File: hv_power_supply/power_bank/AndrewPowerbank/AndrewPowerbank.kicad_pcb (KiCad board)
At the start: 2 copper layers, 48.3 x 30.5 mm, 51 parts, among them J1 NanoFit_RA_TH_02, J2 NanoFit_RA_TH_02, J3 USB-A-S-X-X-SM2, J4 USB-Micro-1981568-1, J5 NanoFit_RA_TH_02, Q1 SSM3K333R, U1 MCP73871T-2CCI_ML, U2 TPS61090RSAR

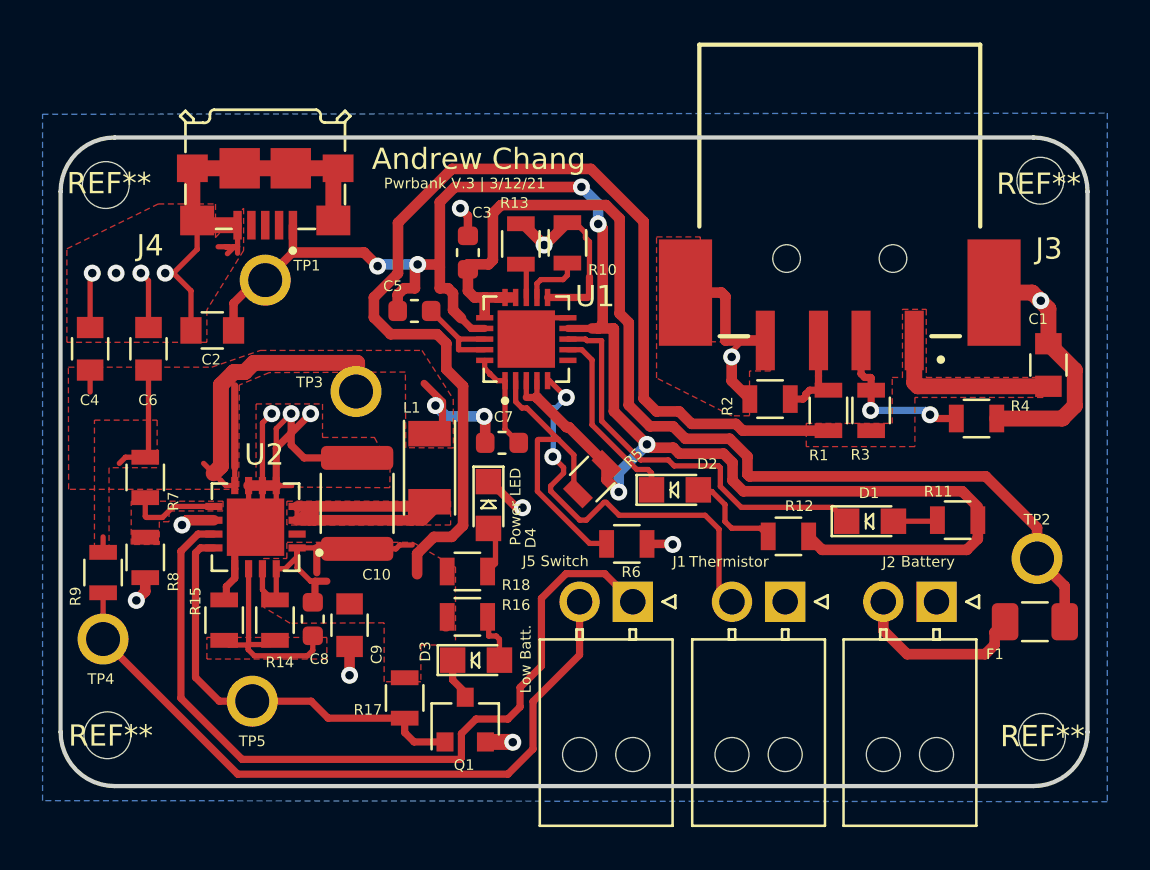
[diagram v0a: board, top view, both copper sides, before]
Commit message: Fix GND connection @ U2 Boost pin 13, 17
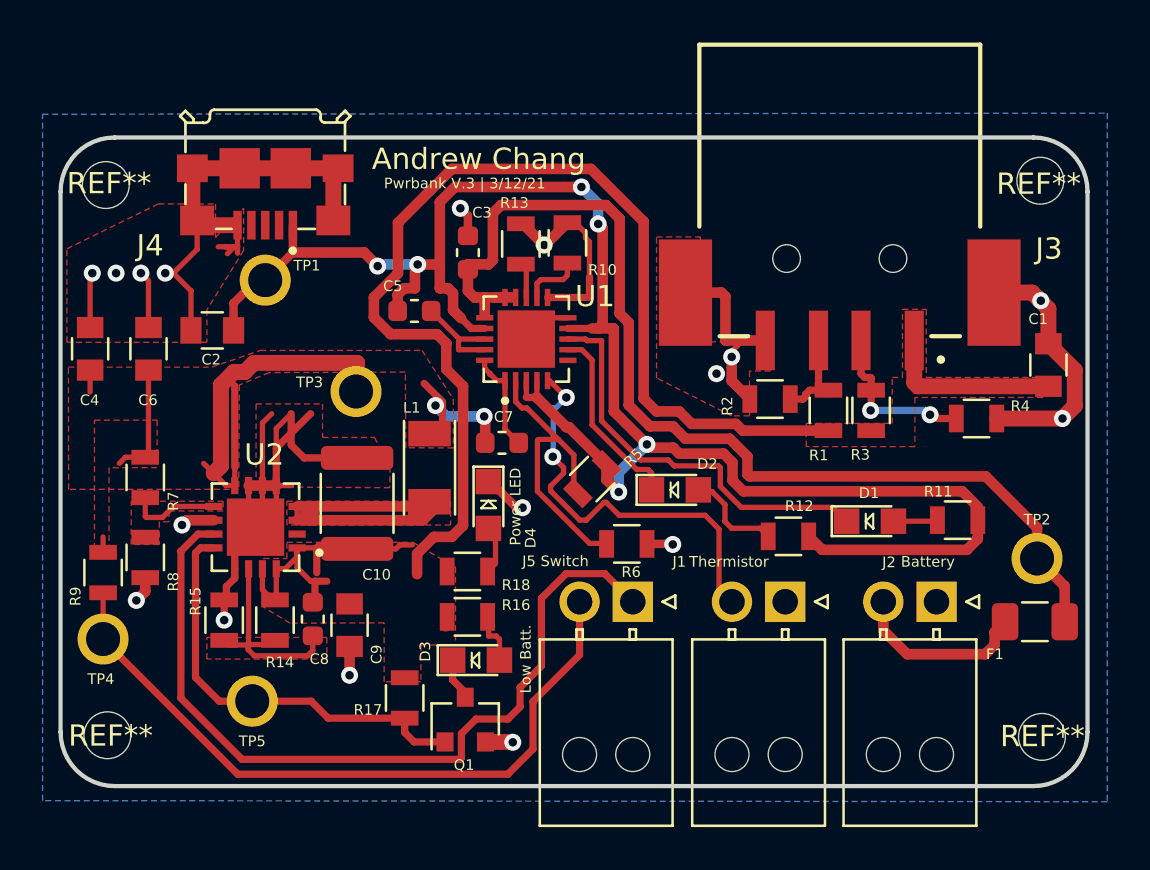
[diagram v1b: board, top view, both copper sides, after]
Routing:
- net GND: track 101.6 -> 102.6 mm

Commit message: Fix issues with board after feedback from Corey.
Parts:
- moved C1 3.60 mm to (74.5, 84.1), turned to 0 degrees
- moved R4 1.65 mm to (73.2, 86.2)
- moved TP3 0.58 mm to (45.5, 84.2)
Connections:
- C5 pad 2: Net-(C5-Pad2) -> GND
- U1 pad 18: Net-(C5-Pad2) -> VBUS
- U1 pad 19: Net-(C5-Pad2) -> VBUS
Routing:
- net GND: track 102.6 -> 83.3 mm, vias 17 -> 25
- net Net-(C5-Pad2): track 4.81 -> 0.00 mm
- net +BATT: track 33.9 -> 30.0 mm
- net +5V: track 78.5 -> 75.2 mm
- net VBUS: track 83.7 -> 84.7 mm

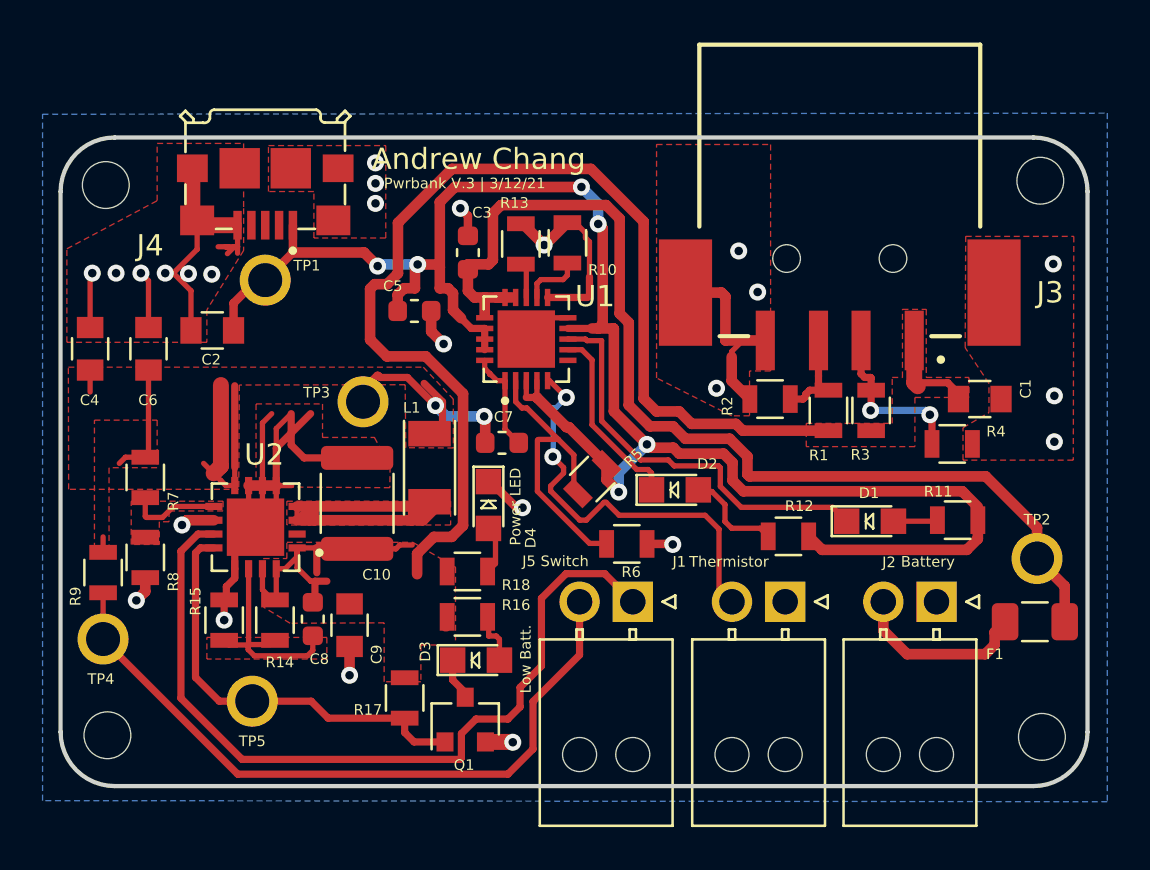
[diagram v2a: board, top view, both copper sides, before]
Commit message: Optimize board addressing Wesley's critiques.
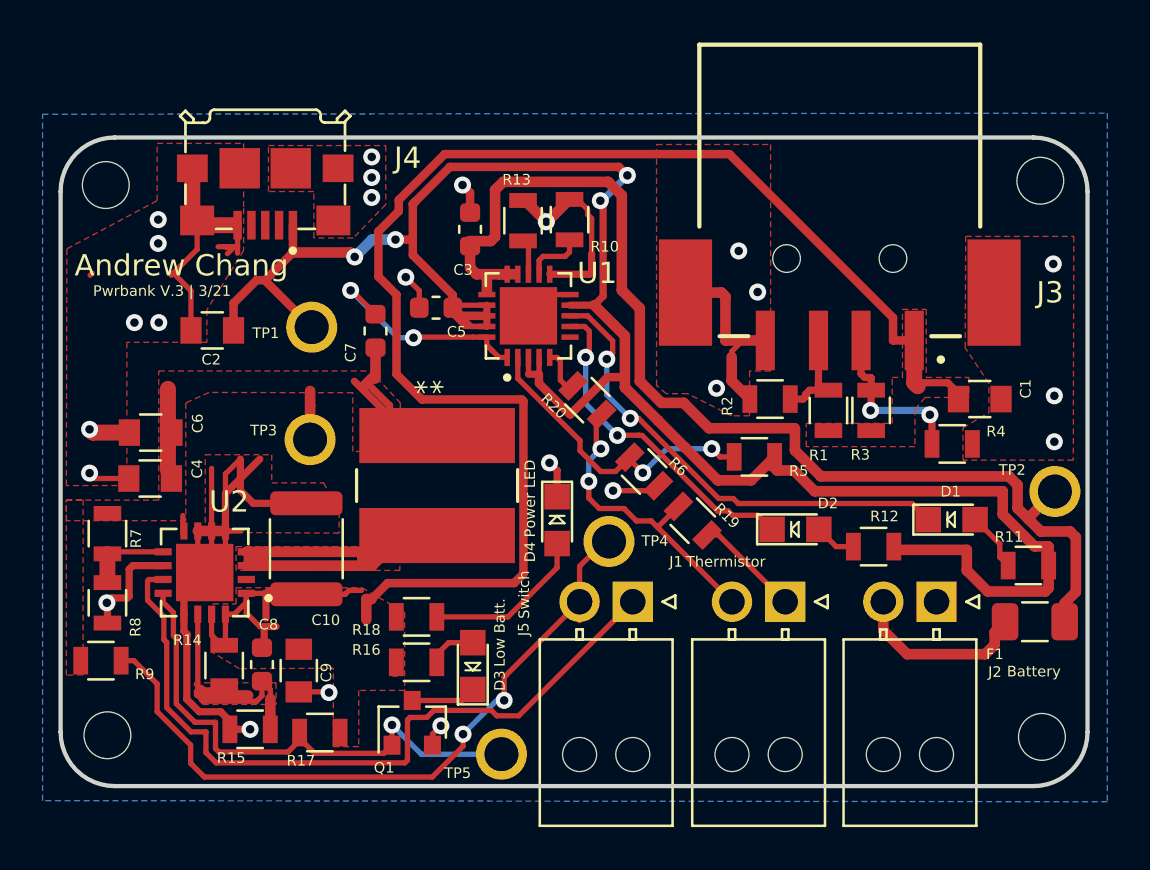
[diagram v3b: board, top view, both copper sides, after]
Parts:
- added R19: R_69.8K, footprints:R_0805_OEM, F.Cu at (61.0, 89.8)
- added R20: R_1.54K, footprints:R_0805_OEM, F.Cu at (56.1, 84.2)
- L1: value L_6.8uH -> L_10uH; footprint footprints:L_100uH_OEM -> footprints:BournsInductor
- moved TP4 24.2 mm to (57.1, 90.8)
- moved TP5 12.0 mm to (52.0, 100.8)
- moved C7 7.94 mm to (46.1, 80.9), turned to 270 degrees
- moved R5 7.69 mm to (63.9, 86.8), turned to 0 degrees
- moved C4 6.72 mm to (35.5, 87.8), turned to 180 degrees
- moved D2 5.96 mm to (65.9, 90.2)
- moved R15 5.27 mm to (40.2, 99.6), turned to 0 degrees
- moved R17 4.31 mm to (43.5, 99.8), turned to 180 degrees
- moved R9 4.14 mm to (33.2, 96.4), turned to 180 degrees
- moved R12 4.03 mm to (69.5, 91.0)
- moved R11 3.95 mm to (76.8, 91.9)
- moved C6 3.94 mm to (35.6, 85.7), turned to 180 degrees
- moved D1 3.84 mm to (73.2, 89.8)
- moved R6 3.50 mm to (58.8, 87.5), turned to 135 degrees
- moved D4 3.30 mm to (54.7, 89.8)
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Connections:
- L1 pad 1: +BATT -> Net-(L1-Pad1)
- L1 pad 2: Net-(L1-Pad2) -> +BATT
- U1 pad 5: /16KThermistor -> Net-(R20-Pad2)
- U2 pad 3: Net-(L1-Pad2) -> Net-(L1-Pad1)
- U2 pad 4: Net-(L1-Pad2) -> Net-(L1-Pad1)
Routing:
- net Net-(L1-Pad2): track 19.7 -> 0.00 mm
- net Net-(L1-Pad1): track 0.00 -> 19.7 mm
- net +BATT: track 30.0 -> 14.3 mm, vias 2 -> 0
- net GND: track 83.3 -> 96.2 mm, vias 25 -> 24
- net VBUS: track 84.7 -> 96.7 mm, vias 6 -> 4
- net +5V: track 75.2 -> 84.9 mm
- net Net-(D2-Pad1): track 8.91 -> 15.9 mm, vias 0 -> 2
- net Net-(C7-Pad1): track 4.81 -> 10.8 mm, vias 0 -> 2
- net Net-(D4-Pad2): track 2.25 -> 7.76 mm
- net /16KThermistor: track 19.7 -> 14.4 mm
- net Net-(Q1-Pad1): track 21.1 -> 25.2 mm, vias 0 -> 1
- net /Battery+: track 50.2 -> 54.1 mm
- net Net-(C8-Pad2): track 10.3 -> 13.9 mm
- net Net-(J5-Pad1): track 38.4 -> 35.1 mm
- net Net-(D1-Pad1): track 19.4 -> 22.7 mm, vias 0 -> 2
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- added copper zone on F.Cu, net Net-(L1-Pad1)
- removed copper zone on F.Cu, net Net-(L1-Pad2)
- removed copper zone on F.Cu, net Net-(R7-Pad1)
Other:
- board text added: "Pwrbank V.3 | 3/21"
- board text removed: "Pwrbank V.3 | 3/12/21"

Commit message: Reformat board to lower USB A, reduce vias.
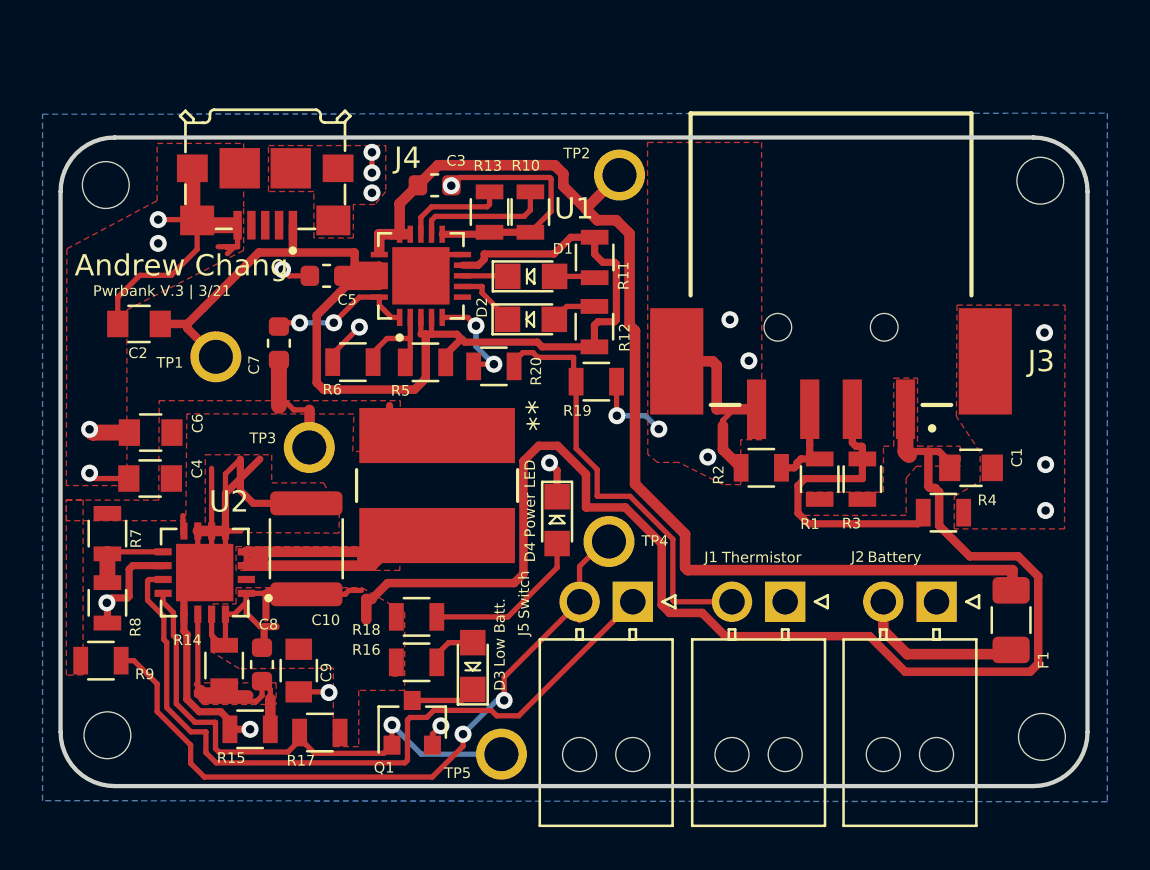
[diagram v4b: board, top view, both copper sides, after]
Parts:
- moved TP2 25.3 mm to (57.6, 73.6)
- moved R11 25.0 mm to (56.4, 77.4), turned to 270 degrees
- moved D1 22.8 mm to (53.4, 78.3)
- moved R12 16.7 mm to (56.4, 80.7), turned to 90 degrees
- moved R5 16.1 mm to (48.5, 82.4)
- moved D2 15.9 mm to (53.4, 80.4)
- moved R6 14.6 mm to (45.1, 82.4), turned to 0 degrees
- moved R19 7.95 mm to (56.5, 83.3), turned to 0 degrees
- moved U1 5.39 mm to (48.3, 78.3)
- moved C5 5.36 mm to (43.8, 78.3)
- moved TP1 4.72 mm to (38.6, 82.1)
- moved R20 4.67 mm to (51.7, 82.6), turned to 180 degrees
- moved C7 4.58 mm to (41.6, 81.5)
- moved C2 3.46 mm to (35.0, 80.6)
- moved R1 3.26 mm to (67.0, 87.9)
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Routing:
- net VBUS: track 96.7 -> 65.8 mm, vias 4 -> 0
- net Net-(D1-Pad1): track 22.7 -> 2.14 mm, vias 2 -> 0
- net Net-(D2-Pad1): track 15.9 -> 2.96 mm, vias 2 -> 0
- net Net-(R5-Pad1): track 14.5 -> 4.68 mm, vias 2 -> 0
- net +BATT: track 14.3 -> 7.28 mm
- net Net-(J3-Pad02): track 9.63 -> 16.2 mm, vias 2 -> 0
- net /16KThermistor: track 14.4 -> 20.4 mm, vias 2 -> 0
- net Net-(C7-Pad1): track 10.8 -> 6.86 mm
- net Net-(R10-Pad1): track 2.82 -> 6.36 mm
- net Net-(R13-Pad1): track 1.62 -> 4.86 mm
- net GND: track 96.2 -> 99.3 mm, vias 24 -> 23
- net Net-(R20-Pad2): track 2.00 -> 4.90 mm, vias 0 -> 2
- net /Battery+: track 54.1 -> 52.4 mm
- net Net-(D1-Pad2): track 2.81 -> 2.00 mm
- net Net-(F1-Pad1): track 8.51 -> 7.90 mm

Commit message: Refill GND plane, fix C7 connection.
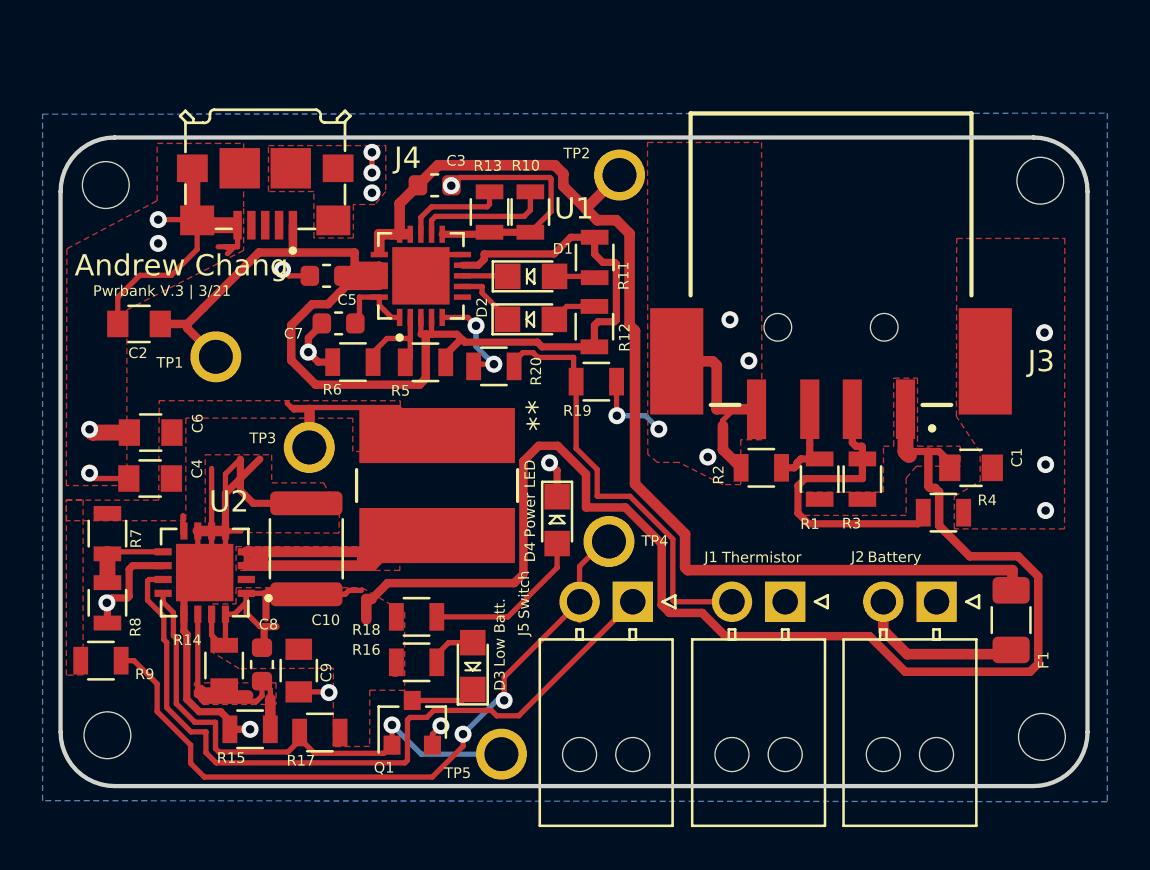
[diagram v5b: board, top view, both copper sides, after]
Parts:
- moved C7 2.96 mm to (44.4, 80.5), turned to 180 degrees
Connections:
- net /16KThermistor renamed /10KThermistor
- C7 pad 2: +BATT -> GND
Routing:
- net +BATT: track 7.28 -> 11.0 mm
- net Net-(C7-Pad1): track 6.86 -> 3.82 mm, vias 2 -> 0
- net VBUS: track 65.8 -> 67.1 mm
- net GND: track 99.3 -> 100.5 mm

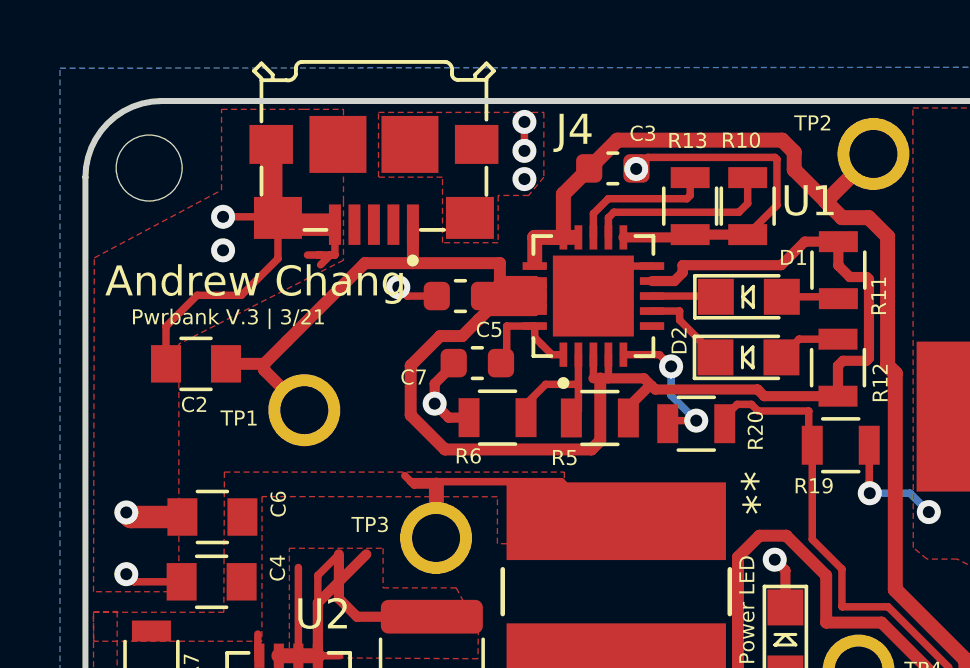
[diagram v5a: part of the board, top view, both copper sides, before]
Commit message: Fix connection to C7.
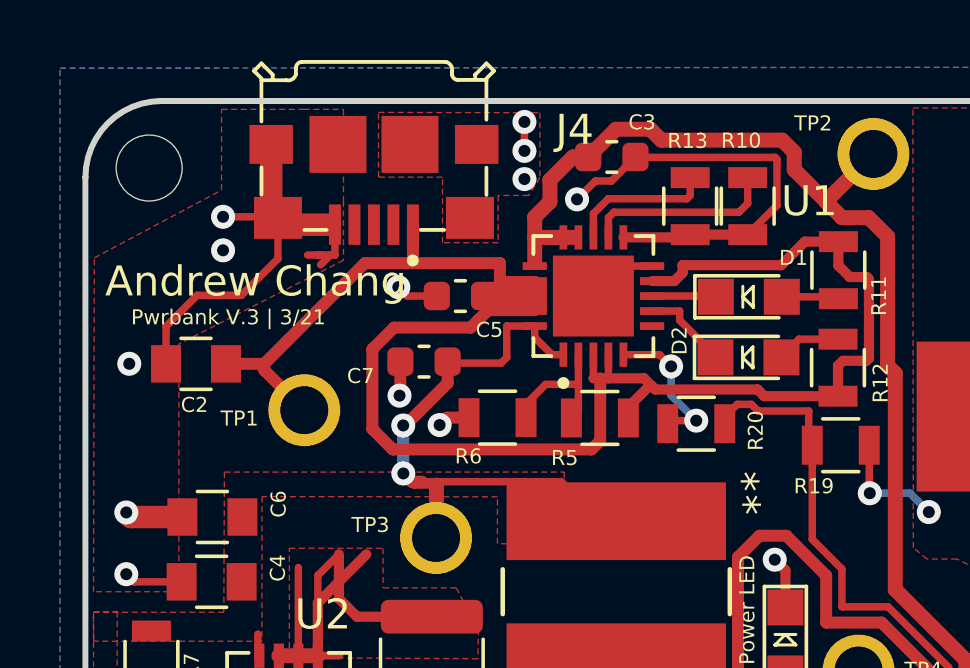
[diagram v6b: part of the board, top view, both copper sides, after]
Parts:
- moved C7 1.78 mm to (42.6, 80.5)
- moved C3 0.38 mm to (48.9, 73.7)
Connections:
- C7 pad 1: Net-(C7-Pad1) -> +BATT
- U1 pad 1: Net-(C7-Pad1) -> +BATT
- U1 pad 20: Net-(C7-Pad1) -> +BATT
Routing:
- net +BATT: track 11.0 -> 21.8 mm, vias 0 -> 2
- net Net-(C7-Pad1): track 3.82 -> 0.00 mm
- net VBUS: track 67.1 -> 70.2 mm
- net GND: track 100.5 -> 101.7 mm, vias 23 -> 25
- net /Battery+: track 52.4 -> 53.6 mm
